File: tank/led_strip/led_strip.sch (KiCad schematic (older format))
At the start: 7 parts, among them J1 Conn_01x04_Male

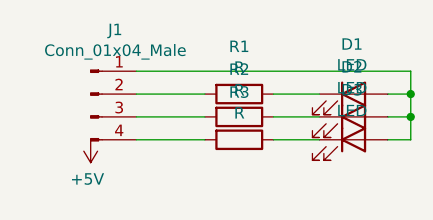
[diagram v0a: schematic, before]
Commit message: LED strip version 0.2
- fix orientation of LED footprints
- fix unconnected traces (DOH.)
- attempt to use local footprint library
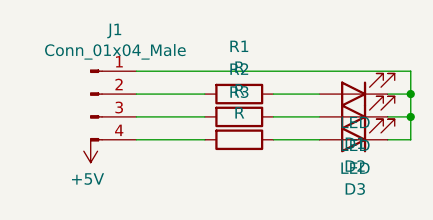
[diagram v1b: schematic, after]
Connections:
- net at R1.1: now also D1.2 (A); no longer D1.1 (K)
- net at R2.1: now also D2.2 (A); no longer D2.1 (K)
- net at R3.1: now also D3.2 (A); no longer D3.1 (K)
- new net: D1.1 (K), D2.1 (K), D3.1 (K), J1.1 (Pin_1)
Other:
- moved on the sheet: D1, D2, D3
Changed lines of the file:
@@
 F 3 "~" H 4850 3050 50  0001 C CNN
 	1    4850 3050
-	1    0    0    -1
+	-1   0    0    1
 $EndComp
 $Comp
@@
 F 3 "~" H 4850 3150 50  0001 C CNN
 	1    4850 3150
-	1    0    0    -1
+	-1   0    0    1
 $EndComp
 $Comp
@@
 F 3 "~" H 4850 3250 50  0001 C CNN
 	1    4850 3250
-	1    0    0    -1
+	-1   0    0    1
 $EndComp
 Wire Wire Line

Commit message: LED version 0.3 - Cannot believe I screwed-up the footprints twice in a row. - Made a little wider for mounting-hole
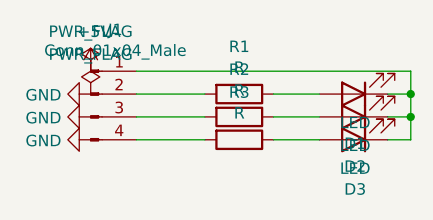
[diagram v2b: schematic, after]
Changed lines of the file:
@@
 Wire Wire Line
 	4500 3150 4700 3150
+Wire Wire Line
+	5100 3050 5100 2950
+Connection ~ 5100 3050
+Wire Wire Line
+	3900 3250 4200 3250
+Wire Wire Line
+	3900 3150 4200 3150
+Wire Wire Line
+	4500 3250 4700 3250
+Wire Wire Line
+	5000 3250 5100 3250
+$Comp
+L power:GND #PWR0101
+U 1 1 614FA139
+P 3700 3250
+F 0 "#PWR0101" H 3700 3000 50  0001 C CNN
+F 1 "GND" V 3705 3122 50  0000 R CNN
+F 2 "" H 3700 3250 50  0001 C CNN
+F 3 "" H 3700 3250 50  0001 C CNN
+	1    3700 3250
+	0    1    1    0
+$EndComp
+$Comp
+L power:GND #PWR0102
+U 1 1 614FA5C0
+P 3700 3150
+F 0 "#PWR0102" H 3700 2900 50  0001 C CNN
+F 1 "GND" V 3705 3022 50  0000 R CNN
+F 2 "" H 3700 3150 50  0001 C CNN
+F 3 "" H 3700 3150 50  0001 C CNN
+	1    3700 3150
+	0    1    1    0
+$EndComp
+$Comp
+L power:GND #PWR0103
+U 1 1 614FAA74
+P 3700 3050
+F 0 "#PWR0103" H 3700 2800 50  0001 C CNN
+F 1 "GND" V 3705 2922 50  0000 R CNN
+F 2 "" H 3700 3050 50  0001 C CNN
+F 3 "" H 3700 3050 50  0001 C CNN
+	1    3700 3050
+	0    1    1    0
+$EndComp
 $Comp
 L Connector:Conn_01x04_Male J1
@@
 	1    0    0    -1
 $EndComp
+Wire Wire Line
+	3900 2950 5100 2950
 $Comp
-L power:+5V #PWR0101
-U 1 1 5EC7F71B
-P 3700 3250
-F 0 "#PWR0101" H 3700 3100 50  0001 C CNN
-F 1 "+5V" H 3715 3423 50  0000 C CNN
-F 2 "" H 3700 3250 50  0001 C CNN
-F 3 "" H 3700 3250 50  0001 C CNN
-	1    3700 3250
-	-1   0    0    1
+L power:PWR_FLAG #FLG0101
+U 1 1 614FFE5A
+P 3700 2950
+F 0 "#FLG0101" H 3700 3025 50  0001 C CNN
+F 1 "PWR_FLAG" H 3700 3123 50  0000 C CNN
+F 2 "" H 3700 2950 50  0001 C CNN
+F 3 "~" H 3700 2950 50  0001 C CNN
+	1    3700 2950
+	1    0    0    -1
+$EndComp
+$Comp
+L power:+5V #PWR0105
+U 1 1 6150140B
+P 3700 2950
+F 0 "#PWR0105" H 3700 2800 50  0001 C CNN
+F 1 "+5V" H 3715 3123 50  0000 C CNN
+F 2 "" H 3700 2950 50  0001 C CNN
+F 3 "" H 3700 2950 50  0001 C CNN
+	1    3700 2950
+	1    0    0    -1
 $EndComp
 Wire Wire Line
-	5100 3050 5100 2950
-Wire Wire Line
-	3900 2950 5100 2950
-Connection ~ 5100 3050
-Wire Wire Line
 	3900 3050 4200 3050
-Wire Wire Line
-	3900 3250 4200 3250
-Wire Wire Line
-	3900 3150 4200 3150
-Wire Wire Line
-	4500 3250 4700 3250
-Wire Wire Line
-	5000 3250 5100 3250
+$Comp
+L power:PWR_FLAG #FLG0102
+U 1 1 61507E52
+P 3700 3050
+F 0 "#FLG0102" H 3700 3125 50  0001 C CNN
+F 1 "PWR_FLAG" H 3700 3223 50  0000 C CNN
+F 2 "" H 3700 3050 50  0001 C CNN
+F 3 "~" H 3700 3050 50  0001 C CNN
+	1    3700 3050
+	1    0    0    -1
+$EndComp
 $EndSCHEMATC

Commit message: Major cleanup. I localized all the footprint and symbol libraries.
I deleted most of the rescue stuff.

I still need to finish-up changes to the turret board.

Now this checkout should work "out of the box".
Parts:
- removed J1: Conn_01x04_Male, Connector_JST:JST_EH_B4B-EH-A_1x04_P2.50mm_Vertical, symbol Connector:Conn_01x04_Male
- added J1: Conn_01x04_Male, custom:JST_EH_B4B-EH-A_1x04_P2.50mm_Vertical, symbol custom:Conn_01x04_Male
- D1, D2, D3: footprint LED_THT:LED_D5.0mm -> custom:LED_D5.0mm; symbol Device:LED -> custom:LED
- R1, R2, R3: footprint Resistor_THT:R_Axial_DIN0207_L6.3mm_D2.5mm_P7.62mm_Horizontal -> custom:R_Axial_DIN0207_L6.3mm_D2.5mm_P7.62mm_Horizontal; symbol Device:R -> custom:R
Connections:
- net at R1.1: now also D1.1 (K); no longer D1.2 (A)
- net at R1.2: now also J1.2 (Pin_2)
- net at R2.1: now also D2.1 (K); no longer D2.2 (A)
- net at R2.2: now also J1.3 (Pin_3)
- net at R3.1: now also D3.1 (K); no longer D3.2 (A)
- net at R3.2: now also J1.4 (Pin_4)
- new net: D1.2 (A), D2.2 (A), D3.2 (A), J1.1 (Pin_1)
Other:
- moved on the sheet: D1, D2, D3
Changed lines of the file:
@@
 $EndDescr
 $Comp
-L Device:R R1
+L custom:R R1
 U 1 1 5EC770AE
 P 4350 3050
 F 0 "R1" V 4143 3050 50  0000 C CNN
 F 1 "R" V 4234 3050 50  0000 C CNN
-F 2 "Resistor_THT:R_Axial_DIN0207_L6.3mm_D2.5mm_P7.62mm_Horizontal" V 4280 3050 50  0001 C CNN
+F 2 "custom:R_Axial_DIN0207_L6.3mm_D2.5mm_P7.62mm_Horizontal" V 4280 3050 50  0001 C CNN
 F 3 "~" H 4350 3050 50  0001 C CNN
 	1    4350 3050
@@
 $EndComp
 $Comp
-L Device:R R2
+L custom:R R2
 U 1 1 5EC7790E
 P 4350 3150
 F 0 "R2" V 4143 3150 50  0000 C CNN
 F 1 "R" V 4234 3150 50  0000 C CNN
-F 2 "Resistor_THT:R_Axial_DIN0207_L6.3mm_D2.5mm_P7.62mm_Horizontal" V 4280 3150 50  0001 C CNN
+F 2 "custom:R_Axial_DIN0207_L6.3mm_D2.5mm_P7.62mm_Horizontal" V 4280 3150 50  0001 C CNN
 F 3 "~" H 4350 3150 50  0001 C CNN
 	1    4350 3150
@@
 $EndComp
 $Comp
-L Device:R R3
+L custom:R R3
 U 1 1 5EC77A2A
 P 4350 3250
 F 0 "R3" V 4143 3250 50  0000 C CNN
 F 1 "R" V 4234 3250 50  0000 C CNN
-F 2 "Resistor_THT:R_Axial_DIN0207_L6.3mm_D2.5mm_P7.62mm_Horizontal" V 4280 3250 50  0001 C CNN
+F 2 "custom:R_Axial_DIN0207_L6.3mm_D2.5mm_P7.62mm_Horizontal" V 4280 3250 50  0001 C CNN
 F 3 "~" H 4350 3250 50  0001 C CNN
 	1    4350 3250
@@
 $EndComp
 $Comp
-L Device:LED D1
+L custom:LED D1
 U 1 1 5EC77B5D
 P 4850 3050
 F 0 "D1" H 4843 3267 50  0000 C CNN
 F 1 "LED" H 4843 3176 50  0000 C CNN
-F 2 "LED_THT:LED_D5.0mm" H 4850 3050 50  0001 C CNN
+F 2 "custom:LED_D5.0mm" H 4850 3050 50  0001 C CNN
 F 3 "~" H 4850 3050 50  0001 C CNN
 	1    4850 3050
-	-1   0    0    1
+	1    0    0    -1
 $EndComp
 $Comp
-L Device:LED D2
+L custom:LED D2
 U 1 1 5EC7AB50
 P 4850 3150
 F 0 "D2" H 4843 3367 50  0000 C CNN
 F 1 "LED" H 4843 3276 50  0000 C CNN
-F 2 "LED_THT:LED_D5.0mm" H 4850 3150 50  0001 C CNN
+F 2 "custom:LED_D5.0mm" H 4850 3150 50  0001 C CNN
 F 3 "~" H 4850 3150 50  0001 C CNN
 	1    4850 3150
-	-1   0    0    1
+	1    0    0    -1
 $EndComp
 $Comp
-L Device:LED D3
+L custom:LED D3
 U 1 1 5EC7AD38
 P 4850 3250
 F 0 "D3" H 4843 3467 50  0000 C CNN
 F 1 "LED" H 4843 3376 50  0000 C CNN
-F 2 "LED_THT:LED_D5.0mm" H 4850 3250 50  0001 C CNN
+F 2 "custom:LED_D5.0mm" H 4850 3250 50  0001 C CNN
 F 3 "~" H 4850 3250 50  0001 C CNN
 	1    4850 3250
-	-1   0    0    1
+	1    0    0    -1
 $EndComp
 Wire Wire Line
@@
 Wire Wire Line
 	5000 3250 5100 3250
+Wire Wire Line
+	3900 2950 5100 2950
+Wire Wire Line
+	3900 3050 4200 3050
 $Comp
-L power:GND #PWR0101
-U 1 1 614FA139
-P 3700 3250
-F 0 "#PWR0101" H 3700 3000 50  0001 C CNN
-F 1 "GND" V 3705 3122 50  0000 R CNN
-F 2 "" H 3700 3250 50  0001 C CNN
-F 3 "" H 3700 3250 50  0001 C CNN
-	1    3700 3250
-	0    1    1    0
-$EndComp
-$Comp
-L power:GND #PWR0102
-U 1 1 614FA5C0
-P 3700 3150
-F 0 "#PWR0102" H 3700 2900 50  0001 C CNN
-F 1 "GND" V 3705 3022 50  0000 R CNN
-F 2 "" H 3700 3150 50  0001 C CNN
-F 3 "" H 3700 3150 50  0001 C CNN
-	1    3700 3150
-	0    1    1    0
-$EndComp
-$Comp
-L power:GND #PWR0103
-U 1 1 614FAA74
-P 3700 3050
-F 0 "#PWR0103" H 3700 2800 50  0001 C CNN
-F 1 "GND" V 3705 2922 50  0000 R CNN
-F 2 "" H 3700 3050 50  0001 C CNN
-F 3 "" H 3700 3050 50  0001 C CNN
-	1    3700 3050
-	0    1    1    0
-$EndComp
-$Comp
-L Connector:Conn_01x04_Male J1
-U 1 1 5EC7F715
+L custom:Conn_01x04_Male J1
+U 1 1 61FCAD98
 P 3700 3050
 F 0 "J1" H 3808 3331 50  0000 C CNN
 F 1 "Conn_01x04_Male" H 3808 3240 50  0000 C CNN
-F 2 "Connector_JST:JST_EH_B4B-EH-A_1x04_P2.50mm_Vertical" H 3700 3050 50  0001 C CNN
-F 3 "~" H 3700 3050 50  0001 C CNN
+F 2 "custom:JST_EH_B4B-EH-A_1x04_P2.50mm_Vertical" H 3700 3050 50  0001 C CNN
+F 3 "" H 3700 3050 50  0001 C CNN
 	1    3700 3050
 	1    0    0    -1
-$EndComp
-Wire Wire Line
-	3900 2950 5100 2950
-$Comp
-L power:PWR_FLAG #FLG0101
-U 1 1 614FFE5A
-P 3700 2950
-F 0 "#FLG0101" H 3700 3025 50  0001 C CNN
-F 1 "PWR_FLAG" H 3700 3123 50  0000 C CNN
-F 2 "" H 3700 2950 50  0001 C CNN
-F 3 "~" H 3700 2950 50  0001 C CNN
-	1    3700 2950
-	1    0    0    -1
-$EndComp
-$Comp
-L power:+5V #PWR0105
-U 1 1 6150140B
-P 3700 2950
-F 0 "#PWR0105" H 3700 2800 50  0001 C CNN
-F 1 "+5V" H 3715 3123 50  0000 C CNN
-F 2 "" H 3700 2950 50  0001 C CNN
-F 3 "" H 3700 2950 50  0001 C CNN
-	1    3700 2950
-	1    0    0    -1
-$EndComp
-Wire Wire Line
-	3900 3050 4200 3050
-$Comp
-L power:PWR_FLAG #FLG0102
-U 1 1 61507E52
-P 3700 3050
-F 0 "#FLG0102" H 3700 3125 50  0001 C CNN
-F 1 "PWR_FLAG" H 3700 3223 50  0000 C CNN
-F 2 "" H 3700 3050 50  0001 C CNN
-F 3 "~" H 3700 3050 50  0001 C CNN
-	1    3700 3050
-	1    0    0    -1
